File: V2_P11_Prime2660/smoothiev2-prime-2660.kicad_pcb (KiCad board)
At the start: 4 copper layers, 110 x 110 mm, 427 parts, among them J1 USB_B, J10 Conn_01x02, J11 Conn_01x02, J12 Conn_01x02, J13 Conn_01x02, J14 Conn_01x02, J15 Conn_01x02, J16 Conn_01x02, J17 Conn_01x02, J18 Conn_01x02, J19 Conn_01x02, J2 USB_A, J20 Conn_01x02, J21 Conn_01x02, J22 Conn_01x02, J23 Conn_01x02, J24 Conn_01x03, J25 Conn_01x03, J26 Conn_01x03, J27 Conn_01x03, J28 Conn_01x03, J29 Conn_01x03, J3 Micro_SD_Card_Det, J30 Conn_01x03_Male, J31 Conn_01x04, J32 Conn_02x05_Odd_Even, J33 Conn_02x05_Odd_Even, J34 Conn_02x05_Odd_Even, J35 Conn_02x05_Odd_Even, J36 Conn_02x05_Odd_Even, J37 Conn_02x05_Odd_Even, J38 Conn_02x05_Odd_Even, J39 Conn_02x05_Odd_Even, J4 RJ45_Hanrun_HR911105A, J40 Conn_02x05_Odd_Even, J41 Conn_ARM_JTAG_SWD_10, J42 Conn_01x02, J43 Conn_01x02, J44 Conn_01x02, J45 Conn_01x02, J5 Screw_Terminal_01x04, J6 Screw_Terminal_01x04, J7 Screw_Terminal_01x04, J8 Screw_Terminal_01x04, J9 Conn_01x02, Q17 WSD3066DN33, Q18 WSD3066DN33, Q19 WSD3066DN33, Q20 WSD3066DN33, Q21 WSD3066DN33, Q22 WSD3066DN33, Q23 CJ2301 S1, Q24 CJ2301 S1, Q25 WSD30L40DN, Q26 2N7002, Q27 MBT3906DW1, Q28 SQ3493EV, Q29 MBT3906DW1, Q30 SQ3493EV, Q31 MBT3906DW1, Q32 SQ3493EV, SW1 SW_Push, SW2 TS-1185EC-C-D-B, U1 LAN8720A, U10 TPD4E1U06DCKR, U11 TPD4E1U06DCKR, U12 LMV324, U13 TPD4E1U06DCKR, U14 TPD4E1U06DCKR, U15 74LCX07, U16 MT9700, U17 TPD4E1U06DCKR, U18 MT9700, U19 MT9700, U2 STM32H745XIHx, U20 MT9700, U21 TPS5430DDA, U22 MT3410L, U23 AP22814AW5, U24 LMV331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

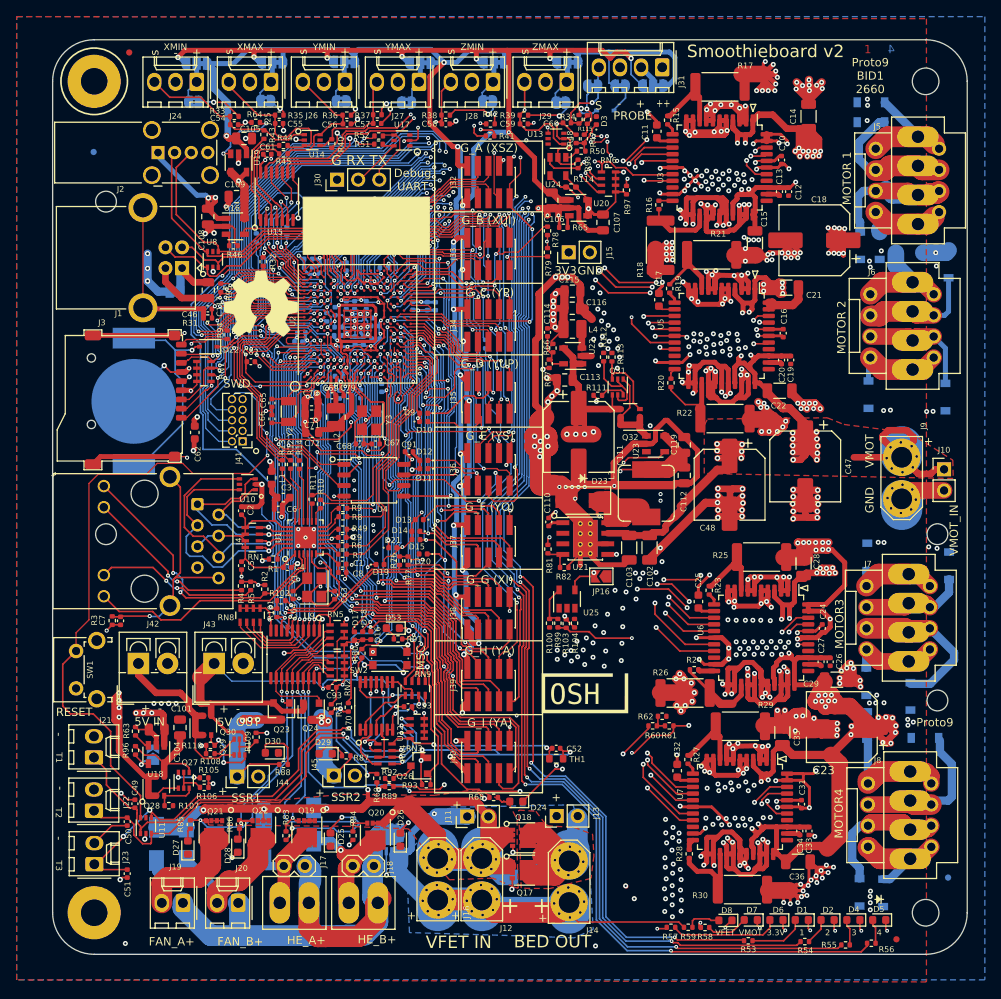
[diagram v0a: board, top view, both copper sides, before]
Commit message: Convert both projects to V8 format fix DRC and ERC (except silkscreen) space out the VFET connectors slightly
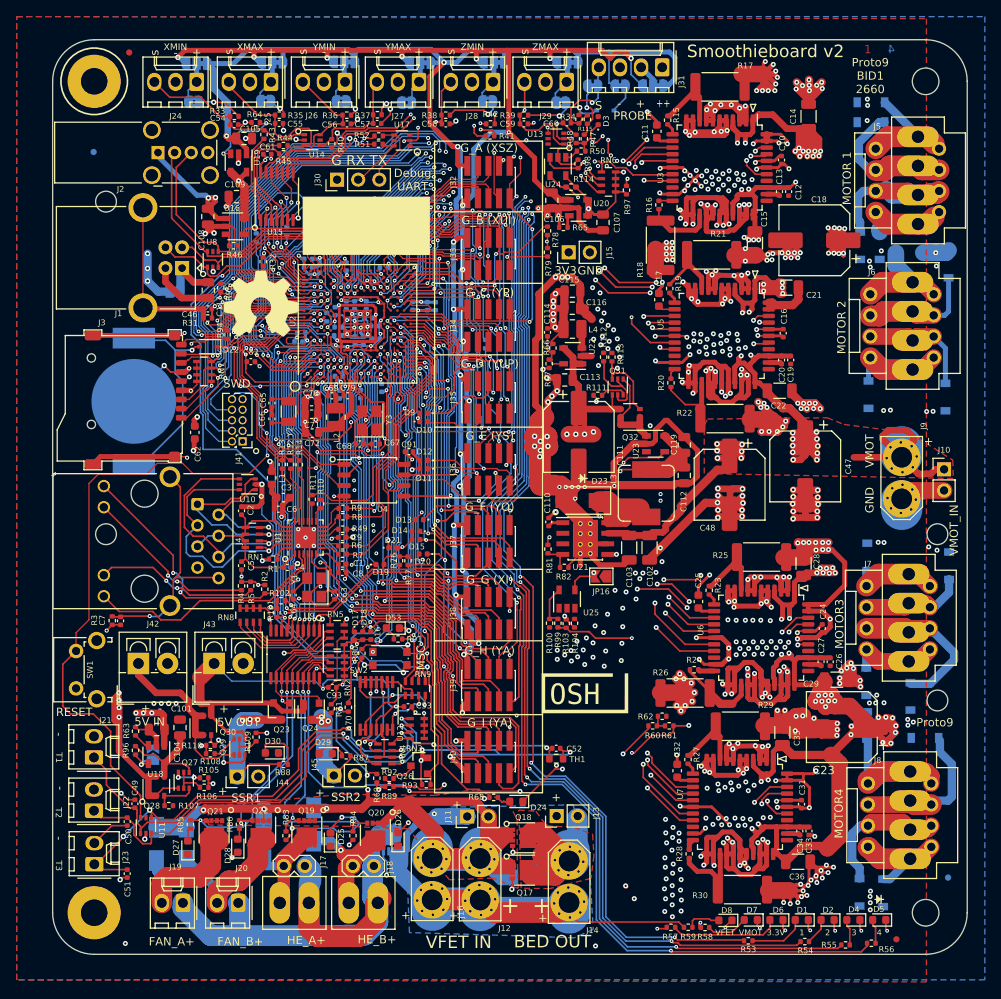
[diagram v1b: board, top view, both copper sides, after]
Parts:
- moved J16 0.68 mm to (145.5, 139.0)
- moved Q25 0.35 mm to (140.6, 134.2)
- moved D26 0.28 mm to (141.4, 134.2)
- moved D3 0.22 mm to (165.4, 47.8)
- moved J12 0.20 mm to (151.2, 139.0)
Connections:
- J41 pad 7: Net-(J41-Pad7) -> unconnected-(J41-KEY-Pad7)
- U10 pad 5: Net-(U10-Pad5) -> unconnected-(U10-Pad5)
- U11 pad 5: Net-(U11-Pad5) -> unconnected-(U11-Pad5)
- U13 pad 3: Net-(U13-Pad3) -> unconnected-(U13-Pad3)
- U13 pad 5: Net-(U13-Pad5) -> unconnected-(U13-Pad5)
- U13 pad 6: Net-(U13-Pad6) -> unconnected-(U13-Pad6)
- U14 pad 5: Net-(U14-Pad5) -> unconnected-(U14-Pad5)
- U17 pad 1: Net-(U17-Pad1) -> unconnected-(U17-Pad1)
- U17 pad 3: Net-(U17-Pad3) -> unconnected-(U17-Pad3)
- U17 pad 5: Net-(U17-Pad5) -> unconnected-(U17-Pad5)
- U2 pad B7: Net-(U2-PadB7) -> unconnected-(U2-PB4-PadB7)
- U2 pad C7: Net-(U2-PadC7) -> unconnected-(U2-PK6-PadC7)
- U2 pad C8: Net-(U2-PadC8) -> unconnected-(U2-PK3-PadC8)
- U2 pad D11: Net-(U2-PadD11) -> unconnected-(U2-PJ12-PadD11)
- U2 pad D14: Net-(U2-PadD14) -> unconnected-(U2-PA10-PadD14)
- U2 pad D6: Net-(U2-PadD6) -> unconnected-(U2-PG15-PadD6)
- U2 pad D7: Net-(U2-PadD7) -> unconnected-(U2-PK7-PadD7)
- U2 pad D8: Net-(U2-PadD8) -> unconnected-(U2-PG14-PadD8)
- U2 pad E12: Net-(U2-PadE12) -> unconnected-(U2-PD1-PadE12)
- U2 pad F13: Net-(U2-PadF13) -> unconnected-(U2-PC7-PadF13)
- U2 pad H1: Net-(U2-PadH1) -> unconnected-(U2-PI12-PadH1)
- U2 pad H2: Net-(U2-PadH2) -> unconnected-(U2-PI13-PadH2)
- U2 pad H3: Net-(U2-PadH3) -> unconnected-(U2-PI14-PadH3)
- U2 pad K16: Net-(U2-PadK16) -> unconnected-(U2-NC-PadK16)
- U2 pad K17: Net-(U2-PadK17) -> unconnected-(U2-NC-PadK17)
- U2 pad L16: Net-(U2-PadL16) -> unconnected-(U2-NC-PadL16)
- U2 pad L17: Net-(U2-PadL17) -> unconnected-(U2-NC-PadL17)
- U2 pad M16: Net-(U2-PadM16) -> unconnected-(U2-NC-PadM16)
- U2 pad M17: Net-(U2-PadM17) -> unconnected-(U2-NC-PadM17)
- U2 pad N17: Net-(U2-PadN17) -> unconnected-(U2-NC-PadN17)
- U2 pad N5: Net-(U2-PadN5) -> unconnected-(U2-PA0-PadN5)
- U2 pad N6: Net-(U2-PadN6) -> unconnected-(U2-PJ0-PadN6)
- U2 pad P5: Net-(U2-PadP5) -> unconnected-(U2-PI15-PadP5)
- U2 pad P6: Net-(U2-PadP6) -> unconnected-(U2-PJ1-PadP6)
- U2 pad R1: Net-(U2-PadR1) -> unconnected-(U2-PC2_C-PadR1)
- U2 pad R11: Net-(U2-PadR11) -> unconnected-(U2-PE15-PadR11)
- U2 pad R12: Net-(U2-PadR12) -> unconnected-(U2-PJ5-PadR12)
- U2 pad R2: Net-(U2-PadR2) -> unconnected-(U2-PC3_C-PadR2)
- U2 pad T11: Net-(U2-PadT11) -> unconnected-(U2-PH6-PadT11)
- U2 pad T2: Net-(U2-PadT2) -> unconnected-(U2-PA1_C-PadT2)
- U21 pad 2: Net-(U21-Pad2) -> unconnected-(U21-NC-Pad2)
- U21 pad 3: Net-(U21-Pad3) -> unconnected-(U21-NC-Pad3)
- U23 pad 3: Net-(U23-Pad3) -> unconnected-(U23-~{FLG}-Pad3)
- U3 pad 37: Net-(U3-Pad37) -> unconnected-(U3-TST_ANA-Pad37)
- U5 pad 37: Net-(U5-Pad37) -> unconnected-(U5-TST_ANA-Pad37)
- U6 pad 37: Net-(U6-Pad37) -> unconnected-(U6-TST_ANA-Pad37)
- U7 pad 37: Net-(U7-Pad37) -> unconnected-(U7-TST_ANA-Pad37)
- U8 pad 5: Net-(U8-Pad5) -> unconnected-(U8-Pad5)
- U9 pad 11: Net-(U9-Pad11) -> unconnected-(U9-Y7-Pad11)
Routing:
- net /VMOT: track 376.3 -> 371.4 mm
- net /5V_IN: track 99.7 -> 96.7 mm
- net /mosfets/GND_FET: track 95.5 -> 97.0 mm
- net /sheet622B088E/COIL_B2: track 57.4 -> 56.0 mm
- net Net-(J17-Pin_1): track 68.7 -> 69.8 mm
- net /MOTSPI_SCK: track 155.6 -> 154.7 mm
- net Net-(J31-Pin_4): track 12.6 -> 12.0 mm
- net /MOTSPI_COPI: track 193.4 -> 192.8 mm, vias 11 -> 9
- net GND: vias 526 -> 530
- net (no net): vias 4 -> 0
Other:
- net class Default removed
- net class HighCurrent removed
- net class Power removed
- net class Signal removed
